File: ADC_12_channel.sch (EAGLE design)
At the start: 165 parts, among them IC1 LM317BD2T, IC2 LM317BD2T, K1 691131710003, K2 691101710002, K3 691101710002, K4 691101710002, K5 691101710002, K6 691101710002, K7 691101710002, K8 691101710002, K9 691101710002, U1 AD7864ASZ-1, U10 TL082D, U12 V_REG_317SMD, U2 AD7864ASZ-1, U3 TL082D, U4 TL082D, U5 TL082D, U6 TL082D, U7 TL082D, U8 TL082D, U9 TL082D, X1 QTE-040

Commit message: ADC-1 Opamp component arrangement FINALIZED!
Uniformly arranged all component of Opamps 1-4
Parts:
- R6, R7, R8, R9: device resistor:R-EU_M0805 -> resistor:R-EU_M1206
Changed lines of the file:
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@@
 <grid distance="0.1" unitdist="inch" unit="inch" style="lines" multiple="1" display="no" altdistance="0.01" altunitdist="inch" altunit="inch"/>
 <layers>
-<layer number="1" name="Top" color="4" fill="1" visible="no" active="no"/>
-<layer number="2" name="Route2" color="1" fill="3" visible="no" active="no"/>
-<layer number="3" name="Route3" color="4" fill="3" visible="no" active="no"/>
-<layer number="4" name="Route4" color="1" fill="4" visible="no" active="no"/>
-<layer number="5" name="Route5" color="4" fill="4" visible="no" active="no"/>
-<layer number="6" name="Route6" color="1" fill="8" visible="no" active="no"/>
-<layer number="7" name="Route7" color="4" fill="8" visible="no" active="no"/>
-<layer number="8" name="Route8" color="1" fill="2" visible="no" active="no"/>
-<layer number="9" name="Route9" color="4" fill="2" visible="no" active="no"/>
-<layer number="10" name="Route10" color="1" fill="7" visible="no" active="no"/>
-<layer number="11" name="Route11" color="4" fill="7" visible="no" active="no"/>
-<layer number="12" name="Route12" color="1" fill="5" visible="no" active="no"/>
-<layer number="13" name="Route13" color="4" fill="5" visible="no" active="no"/>
-<layer number="14" name="Route14" color="1" fill="6" visible="no" active="no"/>
-<layer number="15" name="Route15" color="4" fill="6" visible="no" active="no"/>
-<layer number="16" name="Bottom" color="1" fill="1" visible="no" active="no"/>
-<layer number="17" name="Pads" color="2" fill="1" visible="no" active="no"/>
-<layer number="18" name="Vias" color="2" fill="1" visible="no" active="no"/>
-<layer number="19" name="Unrouted" color="6" fill="1" visible="no" active="no"/>
-<layer number="20" name="Dimension" color="15" fill="1" visible="no" active="no"/>
-<layer number="21" name="tPlace" color="7" fill="1" visible="no" active="no"/>
-<layer number="22" name="bPlace" color="7" fill="1" visible="no" active="no"/>
-<layer number="23" name="tOrigins" color="15" fill="1" visible="no" active="no"/>
-<layer number="24" name="bOrigins" color="15" fill="1" visible="no" active="no"/>
-<layer number="25" name="tNames" color="7" fill="1" visible="no" active="no"/>
-<layer number="26" name="bNames" color="7" fill="1" visible="no" active="no"/>
-<layer number="27" name="tValues" color="7" fill="1" visible="no" active="no"/>
-<layer number="28" name="bValues" color="7" fill="1" visible="no" active="no"/>
+<layer number="1" name="Top" color="4" fill="1" visible="yes" active="no"/>
+<layer number="2" name="Route2" color="1" fill="3" visible="yes" active="no"/>
+<layer number="3" name="Route3" color="4" fill="3" visible="yes" active="no"/>
+<layer number="4" name="Route4" color="1" fill="4" visible="yes" active="no"/>
+<layer number="5" name="Route5" color="4" fill="4" visible="yes" active="no"/>
+<layer number="6" name="Route6" color="1" fill="8" visible="yes" active="no"/>
+<layer number="7" name="Route7" color="4" fill="8" visible="yes" active="no"/>
+<layer number="8" name="Route8" color="1" fill="2" visible="yes" active="no"/>
+<layer number="9" name="Route9" color="4" fill="2" visible="yes" active="no"/>
+<layer number="10" name="Route10" color="1" fill="7" visible="yes" active="no"/>
+<layer number="11" name="Route11" color="4" fill="7" visible="yes" active="no"/>
+<layer number="12" name="Route12" color="1" fill="5" visible="yes" active="no"/>
+<layer number="13" name="Route13" color="4" fill="5" visible="yes" active="no"/>
+<layer number="14" name="Route14" color="1" fill="6" visible="yes" active="no"/>
+<layer number="15" name="Route15" color="4" fill="6" visible="yes" active="no"/>
+<layer number="16" name="Bottom" color="1" fill="1" visible="yes" active="no"/>
+<layer number="17" name="Pads" color="2" fill="1" visible="yes" active="no"/>
+<layer number="18" name="Vias" color="2" fill="1" visible="yes" active="no"/>
+<layer number="19" name="Unrouted" color="6" fill="1" visible="yes" active="no"/>
+<layer number="20" name="Dimension" color="15" fill="1" visible="yes" active="no"/>
+<layer number="21" name="tPlace" color="7" fill="1" visible="yes" active="no"/>
+<layer number="22" name="bPlace" color="7" fill="1" visible="yes" active="no"/>
+<layer number="23" name="tOrigins" color="15" fill="1" visible="yes" active="no"/>
+<layer number="24" name="bOrigins" color="15" fill="1" visible="yes" active="no"/>
+<layer number="25" name="tNames" color="7" fill="1" visible="yes" active="no"/>
+<layer number="26" name="bNames" color="7" fill="1" visible="yes" active="no"/>
+<layer number="27" name="tValues" color="7" fill="1" visible="yes" active="no"/>
+<layer number="28" name="bValues" color="7" fill="1" visible="yes" active="no"/>
 <layer number="29" name="tStop" color="7" fill="3" visible="no" active="no"/>
 <layer number="30" name="bStop" color="7" fill="6" visible="no" active="no"/>
@@
 <layer number="35" name="tGlue" color="7" fill="4" visible="no" active="no"/>
 <layer number="36" name="bGlue" color="7" fill="5" visible="no" active="no"/>
-<layer number="37" name="tTest" color="7" fill="1" visible="no" active="no"/>
-<layer number="38" name="bTest" color="7" fill="1" visible="no" active="no"/>
+<layer number="37" name="tTest" color="7" fill="1" visible="yes" active="no"/>
+<layer number="38" name="bTest" color="7" fill="1" visible="yes" active="no"/>
 <layer number="39" name="tKeepout" color="4" fill="11" visible="no" active="no"/>
 <layer number="40" name="bKeepout" color="1" fill="11" visible="no" active="no"/>
@@
 <layer number="44" name="Drills" color="7" fill="1" visible="no" active="no"/>
 <layer number="45" name="Holes" color="7" fill="1" visible="no" active="no"/>
-<layer number="46" name="Milling" color="3" fill="1" visible="no" active="no"/>
-<layer number="47" name="Measures" color="7" fill="1" visible="no" active="no"/>
-<layer number="48" name="Document" color="7" fill="1" visible="no" active="no"/>
-<layer number="49" name="Reference" color="7" fill="1" visible="no" active="no"/>
-<layer number="50" name="dxf" color="7" fill="1" visible="no" active="no"/>
-<layer number="51" name="tDocu" color="7" fill="1" visible="no" active="no"/>
-<layer number="52" name="bDocu" color="7" fill="1" visible="no" active="no"/>
-<layer number="53" name="tGND_GNDA" color="7" fill="9" visible="no" active="no"/>
-<layer number="54" name="bGND_GNDA" color="1" fill="9" visible="no" active="no"/>
-<layer number="56" name="wert" color="7" fill="1" visible="no" active="no"/>
-<layer number="57" name="tCAD" color="7" fill="1" visible="no" active="no"/>
-<layer number="59" name="tCarbon" color="7" fill="1" visible="no" active="no"/>
-<layer number="60" name="bCarbon" color="7" fill="1" visible="no" active="no"/>
+<layer number="46" name="Milling" color="3" fill="1" visible="yes" active="no"/>
+<layer number="47" name="Measures" color="7" fill="1" visible="yes" active="no"/>
+<layer number="48" name="Document" color="7" fill="1" visible="yes" active="no"/>
+<layer number="49" name="Reference" color="7" fill="1" visible="yes" active="no"/>
+<layer number="50" name="dxf" color="7" fill="1" visible="yes" active="no"/>
+<layer number="51" name="tDocu" color="7" fill="1" visible="yes" active="no"/>
+<layer number="52" name="bDocu" color="7" fill="1" visible="yes" active="no"/>
+<layer number="53" name="tGND_GNDA" color="7" fill="9" visible="yes" active="no"/>
+<layer number="54" name="bGND_GNDA" color="1" fill="9" visible="yes" active="no"/>
+<layer number="56" name="wert" color="7" fill="1" visible="yes" active="no"/>
+<layer number="57" name="tCAD" color="7" fill="1" visible="yes" active="no"/>
+<layer number="59" name="tCarbon" color="7" fill="1" visible="yes" active="no"/>
+<layer number="60" name="bCarbon" color="7" fill="1" visible="yes" active="no"/>
 <layer number="90" name="Modules" color="5" fill="1" visible="yes" active="yes"/>
 <layer number="91" name="Nets" color="2" fill="1" visible="yes" active="yes"/>
@@
 <part name="U2" library="AD7864AS" deviceset="AD7864ASZ-1" device=""/>
 <part name="GND3" library="supply1" deviceset="GND" device="" value="DGND"/>
-<part name="R6" library="resistor" deviceset="R-EU_" device="M0805" value="10k"/>
-<part name="R7" library="resistor" deviceset="R-EU_" device="M0805" value="10k"/>
-<part name="R8" library="resistor" deviceset="R-EU_" device="M0805" value="10k"/>
-<part name="R9" library="resistor" deviceset="R-EU_" device="M0805" value="10k"/>
+<part name="R6" library="resistor" deviceset="R-EU_" device="M1206" value="10k"/>
+<part name="R7" library="resistor" deviceset="R-EU_" device="M1206" value="10k"/>
+<part name="R8" library="resistor" deviceset="R-EU_" device="M1206" value="10k"/>
+<part name="R9" library="resistor" deviceset="R-EU_" device="M1206" value="10k"/>
 <part name="DVDD2" library="supply1" deviceset="VDD" device=""/>
 <part name="VDD2" library="supply1" deviceset="VDD" device=""/>

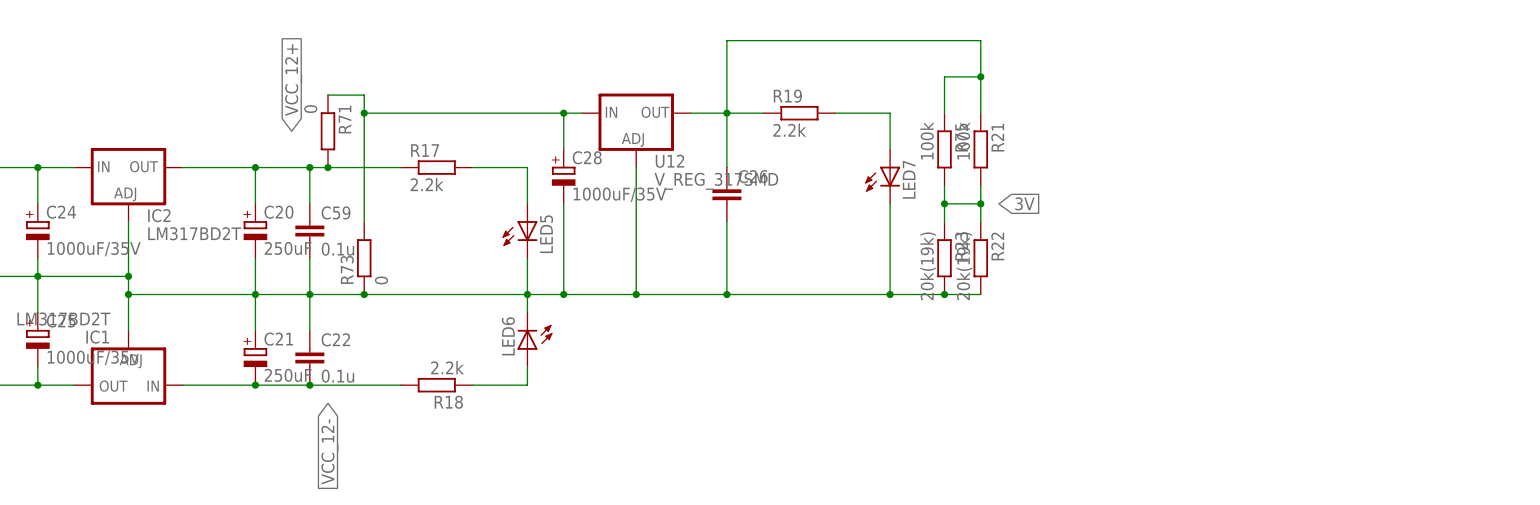
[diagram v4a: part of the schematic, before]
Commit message: Added 5v stage (for Vdd & DVdd)
Finally fixed the supply now. Only, taking out the 12v, 5v and 3v points remaining.
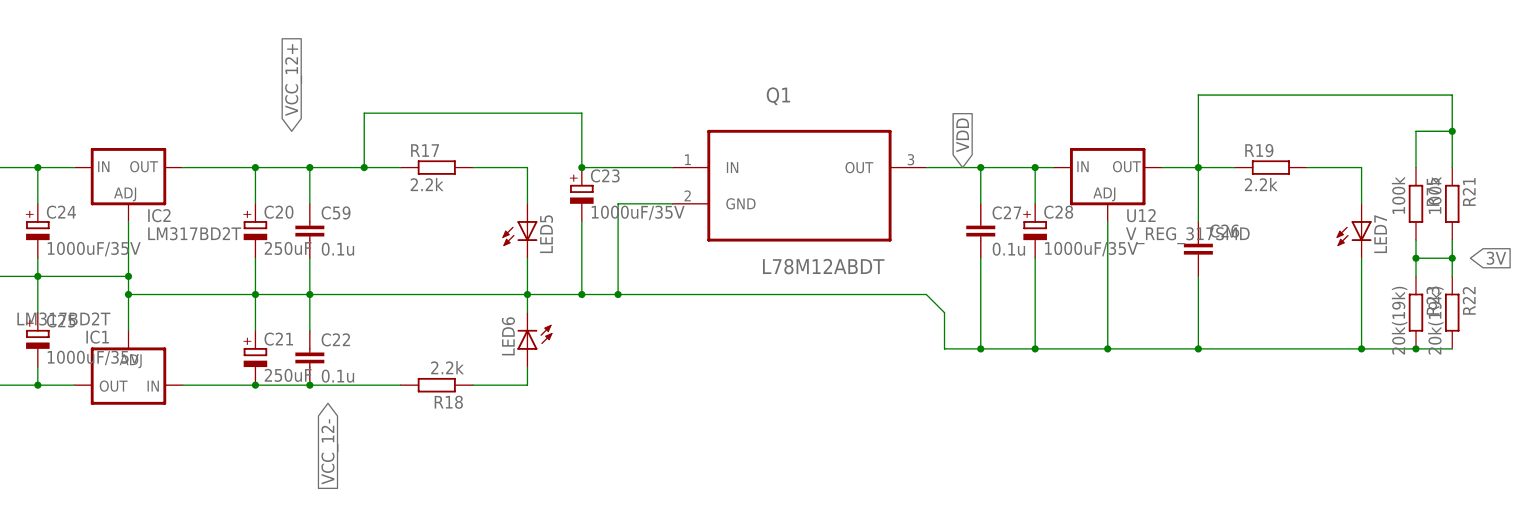
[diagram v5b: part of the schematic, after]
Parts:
- removed R71, R73: 0, resistor:R-EU_M1206
- added C23: 1000uF/35V, rcl:CPOL-EUE5-10.5
- added C27: 0.1u, rcl:C-EUC0603K
- added Q1: L78M12ABDT, ST Microelctronics_By_element14_Batch_1:L78M12ABDT
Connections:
- removed net 5V: C28.+, R71.1, R73.2, U12.IN
- net DGND: now also C23.-, C27.2, Q1.GND; no longer R73.1
- net VCC_12+: now also C23.+, Q1.IN; no longer R71.2
- net VDD: now also C27.1, C28.+, Q1.OUT, U12.IN
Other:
- moved on the sheet: C26, C28, LED7, R19, R21, R22, R23, R75, U12

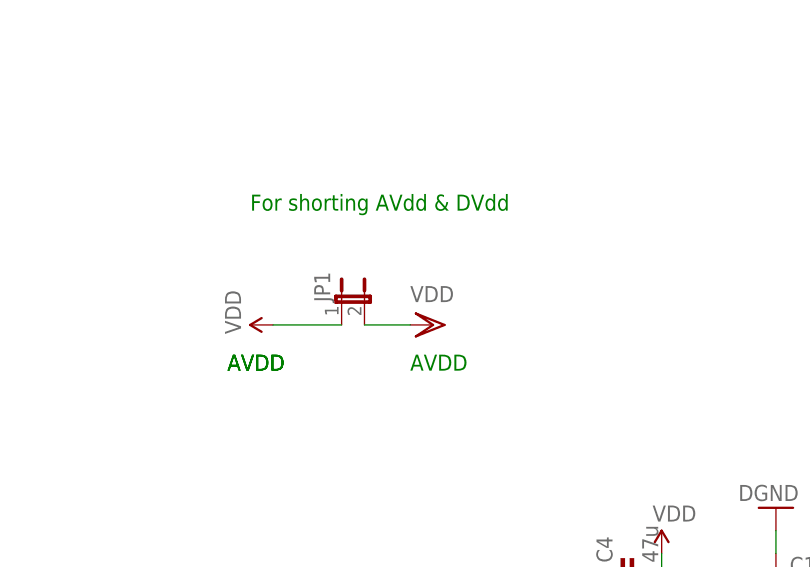
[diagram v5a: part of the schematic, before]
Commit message: joined AVdd and DVdd
It was of no use, due to lack of two seperate regulator IC.
reduced component and simplified the circuit.
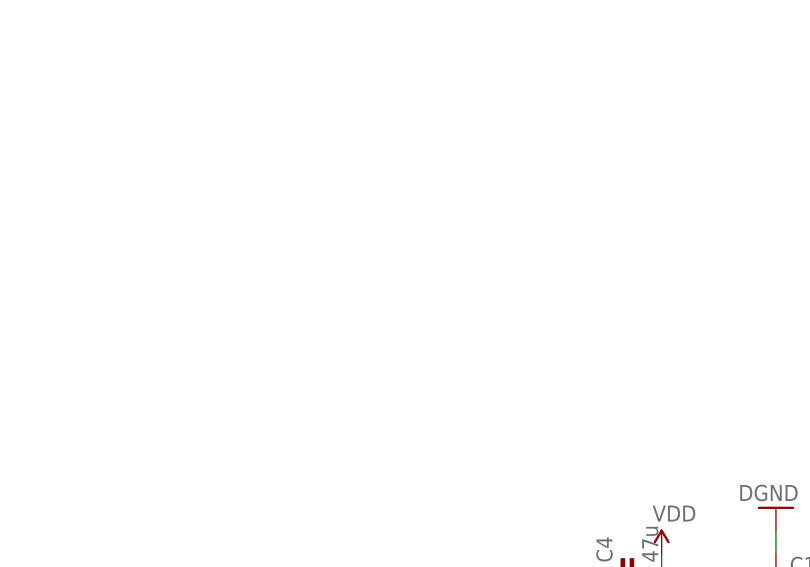
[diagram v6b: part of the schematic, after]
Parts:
- removed JP1: (no value), SparkFun-Retired:JUMPER-2PTH
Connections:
- removed net DVDD: C1.2, C5.2, JP1.2, U1.DVDD, U2.DVDD
- net VDD: now also C1.2, C5.2, U1.DVDD, U2.DVDD; no longer JP1.1
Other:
- note removed: "AVDD"
- note removed: "For shorting AVdd & DVdd"
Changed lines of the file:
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@@
 <part name="C4" library="rcl" deviceset="C-EU" device="C1206K" value="47u"/>
 <part name="SUPPLY1" library="supply2" deviceset="GND" device=""/>
-<part name="JP1" library="SparkFun-Retired" deviceset="JUMPER-2" device="PTH"/>
-<part name="VDD1" library="supply1" deviceset="VDD" device=""/>
-<part name="AVDD1" library="SparkFun-Aesthetics" deviceset="VDD" device=""/>
 <part name="SUPPLY2" library="supply2" deviceset="GND" device=""/>
 <part name="R5" library="resistor" deviceset="R-EU_" device="M1206" value="10k"/>
@@
 <description>ADC Circuit</description>
 <plain>
-<text x="-53.34" y="114.3" size="1.778" layer="91">AVDD</text>
-<text x="-53.34" y="114.3" size="1.778" layer="91">AVDD</text>
-<text x="-33.02" y="114.3" size="1.778" layer="91">AVDD</text>
-<text x="-50.8" y="132.08" size="1.778" layer="91">For shorting AVdd &amp; DVdd </text>
 <text x="-38.1" y="71.12" size="1.778" layer="91">For H/W seq Select</text>
 <text x="-53.34" y="-132.08" size="1.778" layer="91">DO NOT connect!</text>
@@
 <instance part="C4" gate="G$1" x="-10.16" y="91.44" rot="R90"/>
 <instance part="SUPPLY1" gate="GND" x="-17.78" y="88.9" rot="R270"/>
-<instance part="JP1" gate="A" x="-40.64" y="121.92"/>
-<instance part="VDD1" gate="G$1" x="-30.48" y="119.38" rot="R270"/>
-<instance part="AVDD1" gate="VDD" x="-48.26" y="119.38" rot="R90"/>
 <instance part="SUPPLY2" gate="GND" x="-43.18" y="68.58" rot="R180"/>
 <instance part="R5" gate="G$1" x="-43.18" y="50.8" rot="R180"/>
@@
 </segment>
 </net>
-<net name="DVDD" class="0">
-<segment>
-<pinref part="VDD5" gate="G$1" pin="VDD"/>
-<pinref part="U1" gate="A" pin="DVDD"/>
-<wire x1="20.32" y1="86.36" x2="25.4" y2="86.36" width="0.1524" layer="91"/>
-<wire x1="20.32" y1="86.36" x2="7.62" y2="86.36" width="0.1524" layer="91"/>
-<junction x="20.32" y="86.36"/>
-<pinref part="C1" gate="G$1" pin="2"/>
-</segment>
-<segment>
-<pinref part="JP1" gate="A" pin="2"/>
-<pinref part="VDD1" gate="G$1" pin="VDD"/>
-<wire x1="-38.1" y1="119.38" x2="-33.02" y2="119.38" width="0.1524" layer="91"/>
-</segment>
-<segment>
-<pinref part="VDD2" gate="G$1" pin="VDD"/>
-<pinref part="U2" gate="A" pin="DVDD"/>
-<wire x1="20.32" y1="-88.9" x2="25.4" y2="-88.9" width="0.1524" layer="91"/>
-<wire x1="20.32" y1="-88.9" x2="7.62" y2="-88.9" width="0.1524" layer="91"/>
-<junction x="20.32" y="-88.9"/>
-<pinref part="C5" gate="G$1" pin="2"/>
-</segment>
-</net>
 <net name="N$13" class="0">
 <segment>
@@
 </segment>
 <segment>
-<pinref part="JP1" gate="A" pin="1"/>
-<pinref part="AVDD1" gate="VDD" pin="VDD"/>
-<wire x1="-40.64" y1="119.38" x2="-48.26" y2="119.38" width="0.1524" layer="91"/>
-</segment>
-<segment>
 <pinref part="R5" gate="G$1" pin="2"/>
 <pinref part="DVDD1" gate="G$1" pin="VDD"/>
@@
 <label x="734.06" y="274.32" size="1.778" layer="95" rot="R90" xref="yes"/>
 </segment>
-</net>
+<segment>
+<pinref part="VDD5" gate="G$1" pin="VDD"/>
+<pinref part="U1" gate="A" pin="DVDD"/>
+<wire x1="20.32" y1="86.36" x2="25.4" y2="86.36" width="0.1524" layer="91"/>
+<wire x1="20.32" y1="86.36" x2="7.62" y2="86.36" width="0.1524" layer="91"/>
+<junction x="20.32" y="86.36"/>
+<pinref part="C1" gate="G$1" pin="2"/>
+</segment>
+<segment>
+<pinref part="VDD2" gate="G$1" pin="VDD"/>
+<pinref part="U2" gate="A" pin="DVDD"/>
+<wire x1="20.32" y1="-88.9" x2="25.4" y2="-88.9" width="0.1524" layer="91"/>
+<wire x1="20.32" y1="-88.9" x2="7.62" y2="-88.9" width="0.1524" layer="91"/>
+<junction x="20.32" y="-88.9"/>
+<pinref part="C5" gate="G$1" pin="2"/>
+</segment>
+</net>

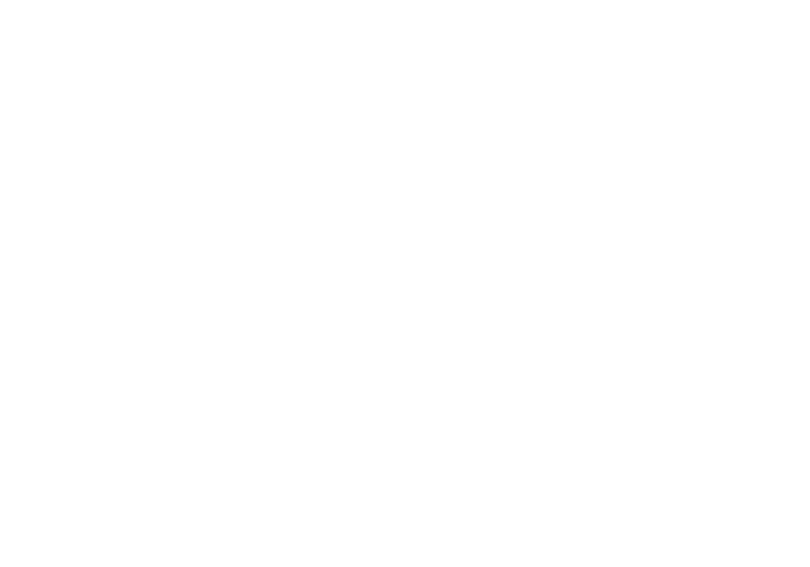
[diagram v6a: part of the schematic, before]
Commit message: Added isolating resistor between DGND & AGND
Layed VDD, DVDD tracks.
Created AGND plane
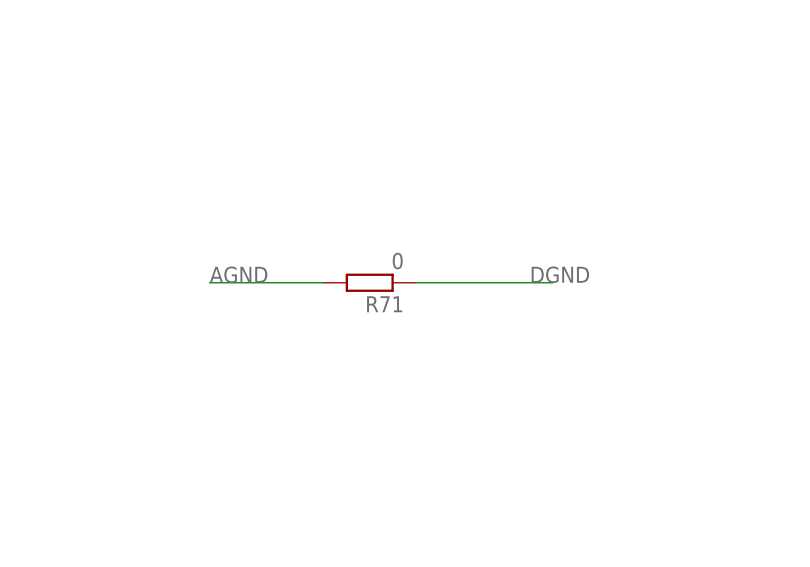
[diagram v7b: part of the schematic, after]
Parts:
- added R71: 0, resistor:R-EU_M1206
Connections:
- net AGND: now also R71.2
- net DGND: now also R71.1
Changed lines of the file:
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@@
 <part name="C23" library="rcl" deviceset="CPOL-EU" device="E5-10.5" value="1000uF/35V"/>
 <part name="C27" library="rcl" deviceset="C-EU" device="C0603K" value="0.1u"/>
+<part name="R71" library="resistor" deviceset="R-EU_" device="M1206" value="0"/>
 </parts>
 <sheets>
@@
 <instance part="C23" gate="G$1" x="680.72" y="271.78"/>
 <instance part="C27" gate="G$1" x="736.6" y="266.7"/>
+<instance part="R71" gate="G$1" x="-243.84" y="177.8" rot="R180"/>
 </instances>
 <busses>
@@
 <junction x="680.72" y="256.54"/>
 </segment>
+<segment>
+<pinref part="R71" gate="G$1" pin="1"/>
+<wire x1="-223.52" y1="177.8" x2="-238.76" y2="177.8" width="0.1524" layer="91"/>
+<label x="-226.06" y="177.8" size="1.778" layer="95"/>
+</segment>
 </net>
 <net name="AGND" class="0">
@@
 <pinref part="SUPPLY15" gate="GND" pin="GND"/>
 </segment>
-</net>
+<segment>
+<pinref part="R71" gate="G$1" pin="2"/>
+<wire x1="-248.92" y1="177.8" x2="-261.62" y2="177.8" width="0.1524" layer="91"/>
+<label x="-261.62" y="177.8" size="1.778" layer="95"/>
+</segment>
+</net>
